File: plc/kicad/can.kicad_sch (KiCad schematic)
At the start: 11 parts, among them CN11 DB2ERC-5.08-4P, J3 Conn_01x02_Pin, SW4 MSK12C02, U18 TCAN337DR

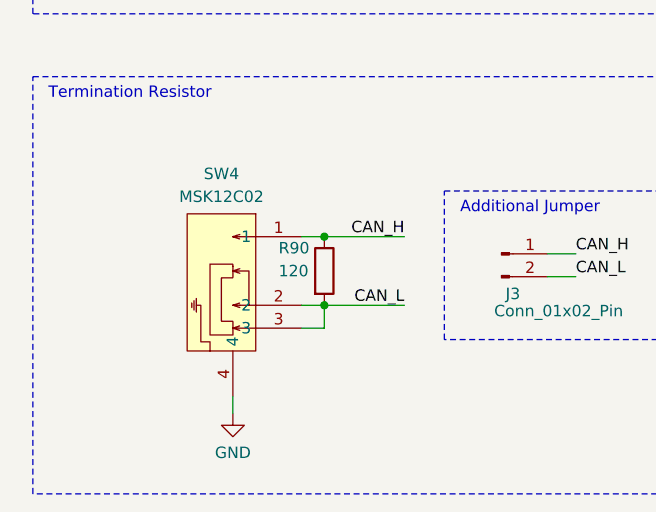
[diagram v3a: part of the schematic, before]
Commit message: Fixed shorting resistors for CAN & RS485
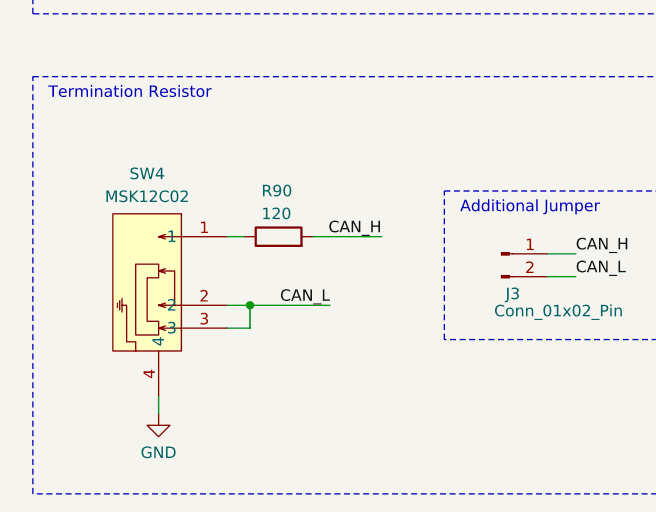
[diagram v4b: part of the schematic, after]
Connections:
- net CAN_H: now also R90.2; no longer R90.1, SW4.1
- net CAN_L: no longer R90.2
- new net: R90.1, SW4.1
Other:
- moved on the sheet: SW4
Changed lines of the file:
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@@
 	)
 	(junction
-		(at 79.375 145.415)
-		(diameter 0)
-		(color 0 0 0 0)
-	)
-	(junction
-		(at 79.375 137.795)
+		(at 71.12 145.415)
 		(diameter 0)
 		(color 0 0 0 0)
@@
 	(wire
 		(pts
+			(xy 78.105 137.795) (xy 85.725 137.795)
+		)
+		(stroke
+			(width 0)
+			(type default)
+		)
+	)
+	(wire
+		(pts
 			(xy 84.455 79.375) (xy 93.98 79.375)
 		)
@@
 	(wire
 		(pts
-			(xy 69.215 157.48) (xy 69.215 155.575)
+			(xy 60.96 157.48) (xy 60.96 155.575)
 		)
 		(stroke
@@
 	(wire
 		(pts
-			(xy 76.835 137.795) (xy 79.375 137.795)
-		)
-		(stroke
-			(width 0)
-			(type default)
-		)
-	)
-	(wire
-		(pts
-			(xy 79.375 147.955) (xy 79.375 145.415)
+			(xy 71.12 147.955) (xy 71.12 145.415)
 		)
 		(stroke
@@
 	(wire
 		(pts
-			(xy 79.375 145.415) (xy 88.265 145.415)
+			(xy 71.12 145.415) (xy 80.01 145.415)
 		)
 		(stroke
@@
 	(wire
 		(pts
+			(xy 70.485 137.795) (xy 68.58 137.795)
+		)
+		(stroke
+			(width 0)
+			(type default)
+		)
+	)
+	(wire
+		(pts
 			(xy 220.345 152.4) (xy 245.745 152.4)
 		)
@@
 	(wire
 		(pts
-			(xy 79.375 137.795) (xy 88.265 137.795)
-		)
-		(stroke
-			(width 0)
-			(type default)
-		)
-	)
-	(wire
-		(pts
-			(xy 76.835 145.415) (xy 79.375 145.415)
+			(xy 68.58 145.415) (xy 71.12 145.415)
 		)
 		(stroke
@@
 	(wire
 		(pts
-			(xy 76.835 147.955) (xy 79.375 147.955)
+			(xy 68.58 147.955) (xy 71.12 147.955)
 		)
 		(stroke
@@
 		)
 	)
+	(label "CAN_H"
+		(at 85.725 137.795 180)
+		(effects
+			(font
+				(size 1.27 1.27)
+			)
+			(justify right bottom)
+		)
+	)
 	(label "CAN_TX"
 		(at 139.7 79.375 180)
@@
 	)
 	(label "CAN_L"
-		(at 88.265 145.415 180)
+		(at 80.01 145.415 180)
 		(effects
 			(font
@@
 	(label "CAN_RX"
 		(at 139.7 86.995 180)
-		(effects
-			(font
-				(size 1.27 1.27)
-			)
-			(justify right bottom)
-		)
-	)
-	(label "CAN_H"
-		(at 88.265 137.795 180)
 		(effects
 			(font
@@
 	(symbol
 		(lib_id "LibrePLC32:MSK12C02")
-		(at 70.485 145.415 270)
+		(at 62.23 145.415 270)
 		(unit 1)
 		(body_style 1)
@@
 		(fields_autoplaced yes)
 		(property "Reference" "SW4"
-			(at 67.945 130.81 90)
+			(at 59.69 130.81 90)
 			(show_name no)
 			(do_not_autoplace no)
@@
 		)
 		(property "Value" "MSK12C02"
-			(at 67.945 133.35 90)
+			(at 59.69 133.35 90)
 			(show_name no)
 			(do_not_autoplace no)
@@
 		)
 		(property "Footprint" "LibrePLC32:SW-TH_MSK12C02"
-			(at 61.595 145.415 0)
+			(at 53.34 145.415 0)
 			(hide yes)
 			(show_name no)
@@
 		)
 		(property "Datasheet" "https://lcsc.com/product-detail/Toggle-Switches_SHOU-HAN-MSK12C02_C431540.html"
-			(at 59.055 145.415 0)
+			(at 50.8 145.415 0)
 			(hide yes)
 			(show_name no)
@@
 		)
 		(property "Description" ""
-			(at 70.485 145.415 0)
+			(at 62.23 145.415 0)
 			(hide yes)
 			(show_name no)
@@
 		)
 		(property "Manufacturer" "SHOU HAN(首韩)"
-			(at 56.515 145.415 0)
+			(at 48.26 145.415 0)
 			(hide yes)
 			(show_name no)
@@
 		)
 		(property "MPN" "MSK12C02"
-			(at 53.975 145.415 0)
+			(at 45.72 145.415 0)
 			(hide yes)
 			(show_name no)
@@
 		)
 		(property "LCSC Part" "C431540"
-			(at 51.435 145.415 0)
+			(at 43.18 145.415 0)
 			(hide yes)
 			(show_name no)
@@
 	(symbol
 		(lib_id "power:GND")
-		(at 69.215 157.48 0)
+		(at 60.96 157.48 0)
 		(unit 1)
 		(body_style 1)
@@
 		(fields_autoplaced yes)
 		(property "Reference" "#PWR0203"
-			(at 69.215 163.83 0)
+			(at 60.96 163.83 0)
 			(hide yes)
 			(show_name no)
@@
 		)
 		(property "Value" "GND"
-			(at 69.215 161.798 0)
+			(at 60.96 161.798 0)
 			(show_name no)
 			(do_not_autoplace no)
@@
 		)
 		(property "Footprint" ""
-			(at 69.215 157.48 0)
+			(at 60.96 157.48 0)
 			(hide yes)
 			(show_name no)
@@
 		)
 		(property "Datasheet" ""
-			(at 69.215 157.48 0)
+			(at 60.96 157.48 0)
 			(hide yes)
 			(show_name no)
@@
 		)
 		(property "Description" "Power symbol creates a global label with name \"GND\" , ground"
-			(at 69.215 157.48 0)
+			(at 60.96 157.48 0)
 			(hide yes)
 			(show_name no)
@@
 	(symbol
 		(lib_id "Device:R")
-		(at 79.375 141.605 0)
-		(unit 1)
-		(body_style 1)
-		(exclude_from_sim no)
-		(in_bom yes)
-		(on_board yes)
-		(in_pos_files yes)
-		(dnp no)
-		(property "Reference" "R90"
-			(at 74.295 139.065 0)
-			(show_name no)
-			(do_not_autoplace no)
-			(effects
-				(font
-					(size 1.27 1.27)
-				)
-				(justify left)
-			)
-		)
-		(property "Value" "120"
-			(at 74.295 141.605 0)
-			(show_name no)
-			(do_not_autoplace no)
-			(effects
-				(font
-					(size 1.27 1.27)
-				)
-				(justify left)
-			)
-		)
-		(property "Footprint" "Resistor_SMD:R_0603_1608Metric"
-			(at 77.597 141.605 90)
-			(hide yes)
-			(show_name no)
-			(do_not_autoplace no)
-			(effects
-				(font
-					(size 1.27 1.27)
-				)
-			)
-		)
-		(property "Datasheet" ""
-			(at 79.375 141.605 0)
-			(hide yes)
-			(show_name no)
-			(do_not_autoplace no)
-			(effects
-				(font
-					(size 1.27 1.27)
-				)
-			)
-		)
-		(property "Description" "Resistor"
-			(at 79.375 141.605 0)
-			(hide yes)
-			(show_name no)
-			(do_not_autoplace no)
-			(effects
-				(font
-					(size 1.27 1.27)
-				)
-			)
-		)
-		(pin "2"
-		)
-		(pin "1"
-		)
-		(instances
-			(project "LibrePLC32"
-				(path "/ef4c1a27-85a3-413a-9f93-a41c4f97eee5/1f15b1b2-5031-4e14-8391-148d71dbf666"
-					(reference "R90")
-					(unit 1)
-				)
-			)
-		)
-	)
-	(symbol
-		(lib_id "Device:R")
 		(at 122.555 86.995 90)
 		(unit 1)
@@
 					(unit 1)
 				)
+			)
+		)
+	)
+	(symbol
+		(lib_id "Device:R")
+		(at 74.295 137.795 90)
+		(unit 1)
+		(body_style 1)
+		(exclude_from_sim no)
+		(in_bom yes)
+		(on_board yes)
+		(in_pos_files yes)
+		(dnp no)
+		(property "Reference" "R90"
+			(at 72.39 132.715 90)
+			(show_name no)
+			(do_not_autoplace no)
+			(effects
+				(font
+					(size 1.27 1.27)
+				)
+				(justify right)
+			)
+		)
+		(property "Value" "120"
+			(at 72.39 135.255 90)
+			(show_name no)
+			(do_not_autoplace no)
+			(effects
+				(font
+					(size 1.27 1.27)
+				)
+				(justify right)
+			)
+		)
+		(property "Footprint" "Resistor_SMD:R_0603_1608Metric"
+			(at 74.295 139.573 90)
+			(hide yes)
+			(show_name no)
+			(do_not_autoplace no)
+			(effects
+				(font
+					(size 1.27 1.27)
+				)
+			)
+		)
+		(property "Datasheet" ""
+			(at 74.295 137.795 0)
+			(hide yes)
+			(show_name no)
+			(do_not_autoplace no)
+			(effects
+				(font
+					(size 1.27 1.27)
+				)
+			)
+		)
+		(property "Description" "Resistor"
+			(at 74.295 137.795 0)
+			(hide yes)
+			(show_name no)
+			(do_not_autoplace no)
+			(effects
+				(font
+					(size 1.27 1.27)
+				)
+			)
+		)
+		(pin "2"
+		)
+		(pin "1"
+		)
+		(instances
+			(project "LibrePLC32"
+				(path "/ef4c1a27-85a3-413a-9f93-a41c4f97eee5/1f15b1b2-5031-4e14-8391-148d71dbf666"
+					(reference "R90")
+					(unit 1)
+				)

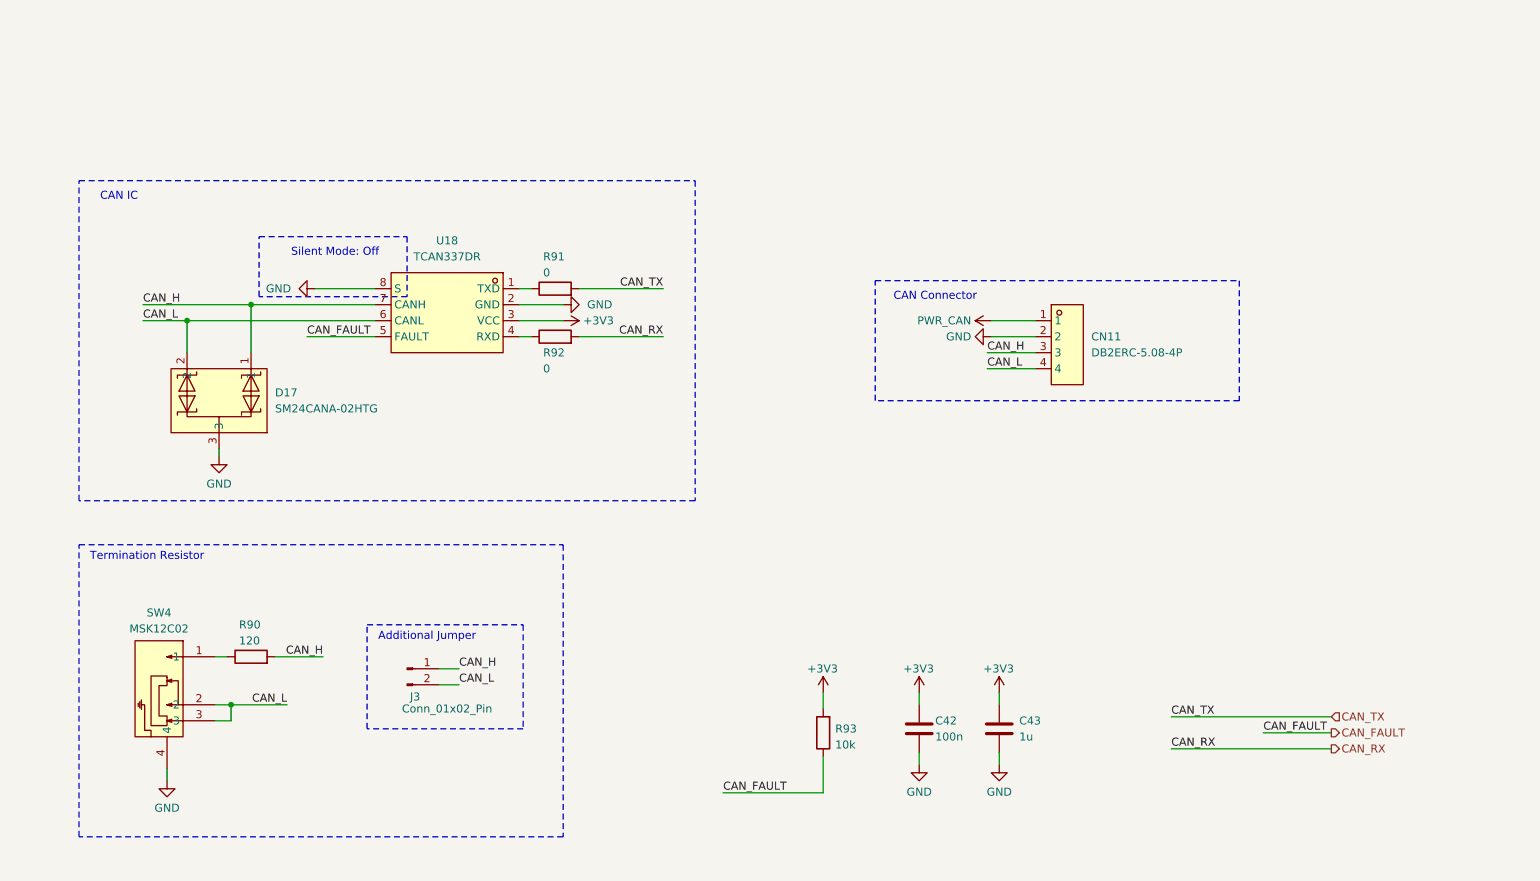
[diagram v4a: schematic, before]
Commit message: Added isolated CAN bus
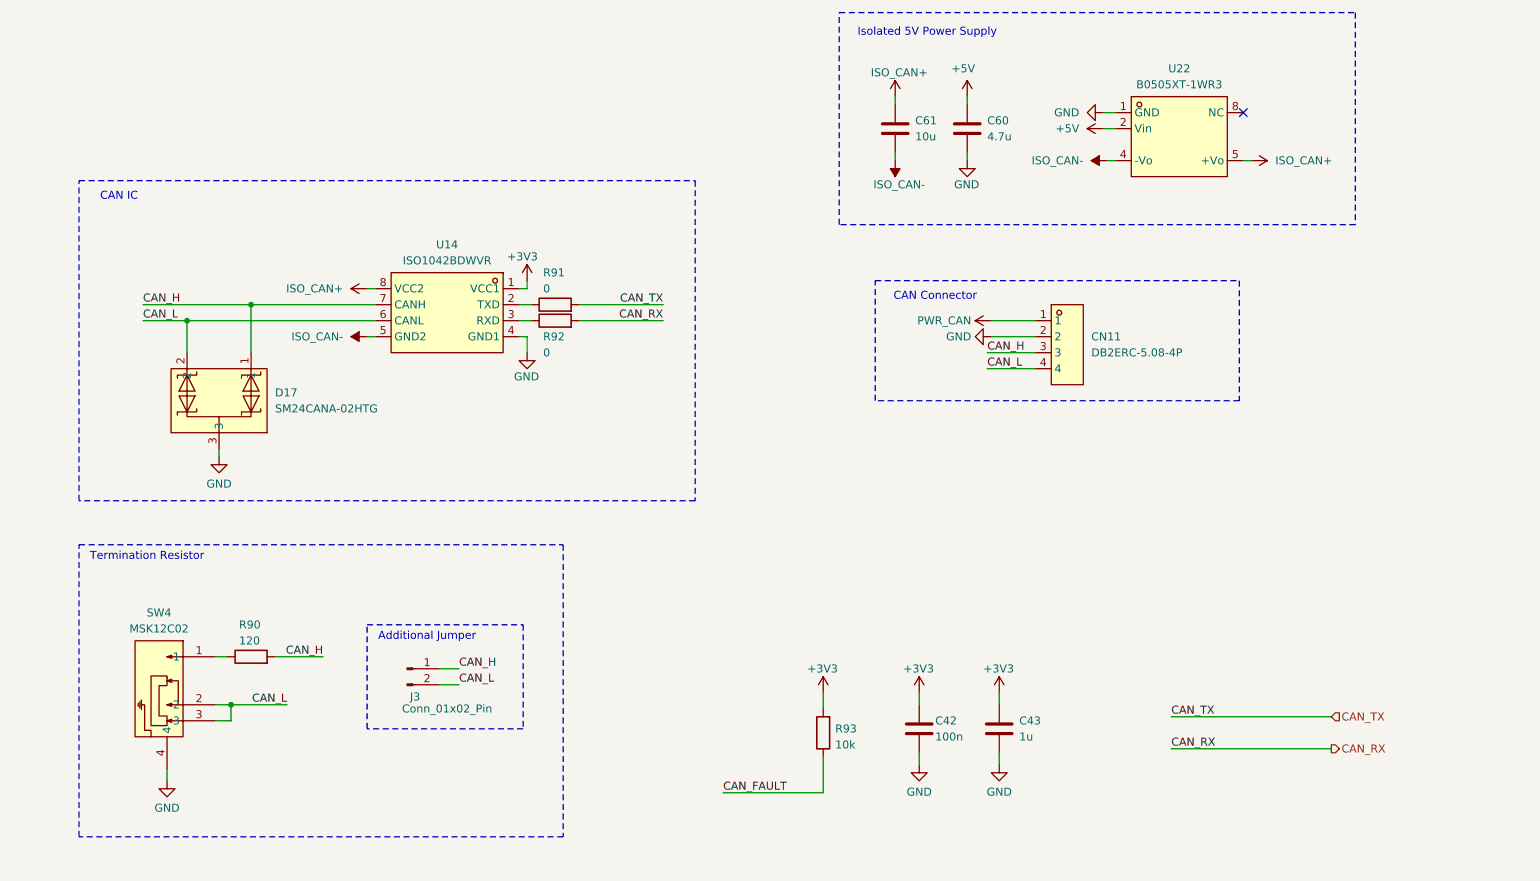
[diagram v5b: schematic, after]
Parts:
- removed U18: TCAN337DR, LibrePLC32:SOIC-8_L4.9-W3.9-P1.27-LS6.0-BL, symbol LibrePLC32:TCAN337DR
- added C60: 4.7u, Capacitor_SMD:C_0603_1608Metric, symbol Device:C
- added C61: 10u, Capacitor_SMD:C_0603_1608Metric, symbol Device:C
- added U14: ISO1042BDWVR, LibrePLC32:SOIC-8_L5.9-W7.5-P1.27-LS11.5-BL, symbol LibrePLC32:ISO1042BDWVR
- added U22: B0505XT-1WR3, LibrePLC32:PWRM-SMD_BXXXXXT-1WR3, symbol LibrePLC32:B0505XT-1WR3_C5369529
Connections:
- net +3V3: now also U14.1 (VCC1)
- net CAN_H: now also U14.7 (CANH)
- net CAN_L: now also U14.6 (CANL)
- net GND: now also C60.2, U14.4 (GND1), U22.1 (GND)
- net at R91.1: now also U14.2 (TXD)
- net at R92.1: now also U14.3 (RXD)
- new net +5V: C60.1, U22.2 (Vin)
- new net ISO_CAN+: C61.1, U14.8 (VCC2), U22.5 (+Vo)
- new net ISO_CAN-: C61.2, U14.5 (GND2), U22.4 (-Vo)
- no-connect marks 0 -> 1
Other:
- note added: "Isolated 5V Power Supply"
- note removed: "Silent Mode: Off"
- moved on the sheet: R91, R92

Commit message: Added isolated RS-485
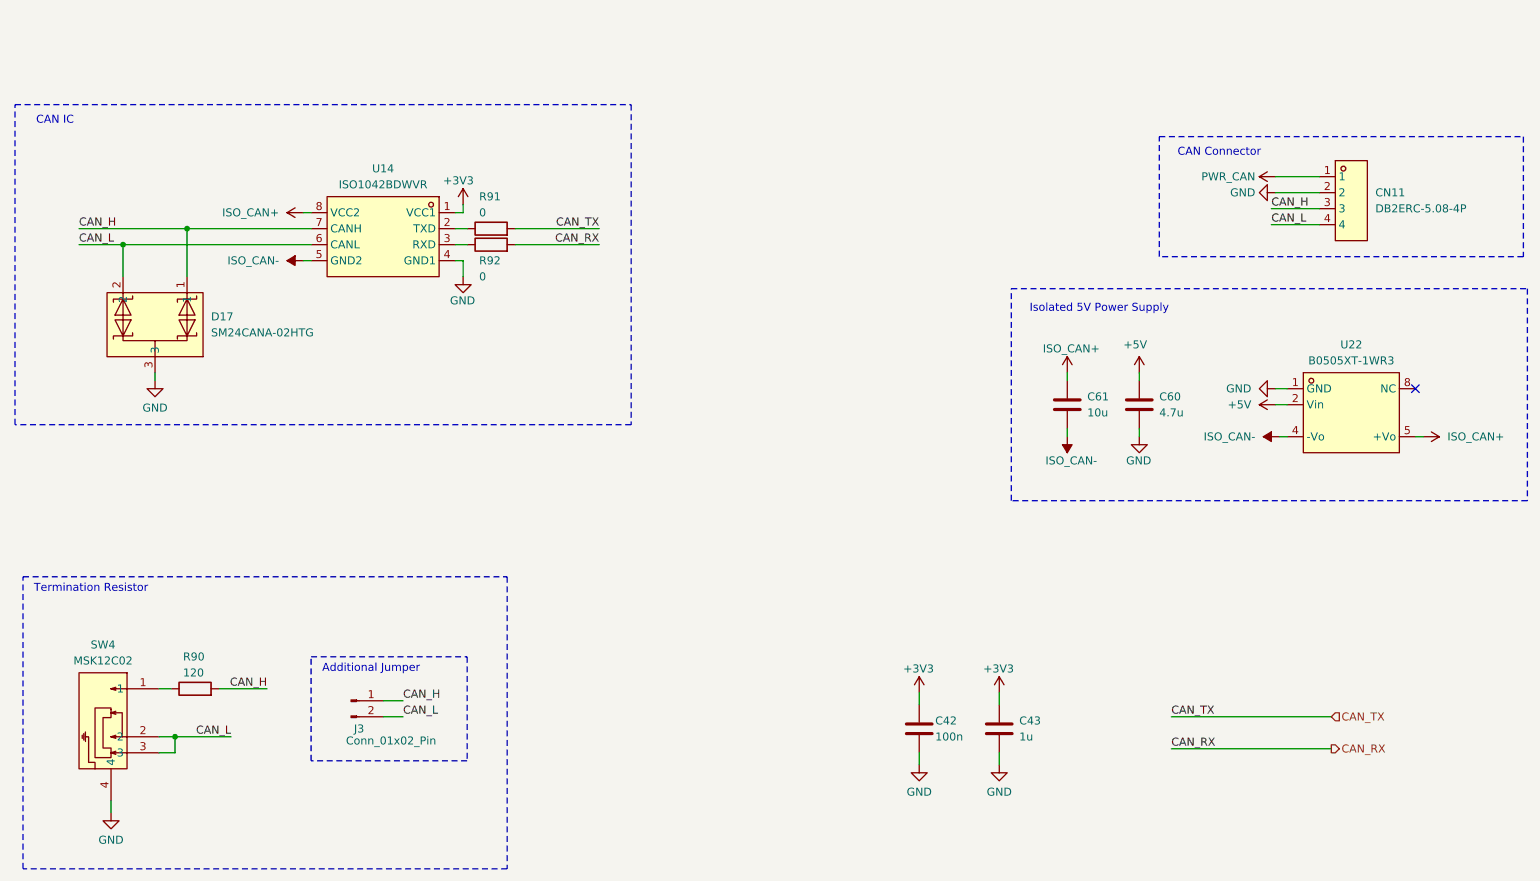
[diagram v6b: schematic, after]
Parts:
- removed R93: 10k, Resistor_SMD:R_0603_1608Metric, symbol Device:R
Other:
- moved on the sheet: C60, C61, CN11, D17, J3, R90, R91, R92, SW4, U14, U22
